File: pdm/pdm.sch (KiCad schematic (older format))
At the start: 30 parts, among them J1 Conn_01x04_Male, J2 Conn_01x12_Male, J3 Conn_01x04_Female, J4 Conn_01x06_Female, M1 Fan, M2 Fan, Q11 Q_PMOS_DSG, SW1 SW_Push, U2 SN65HVD233, U3 STM32F042G6Ux

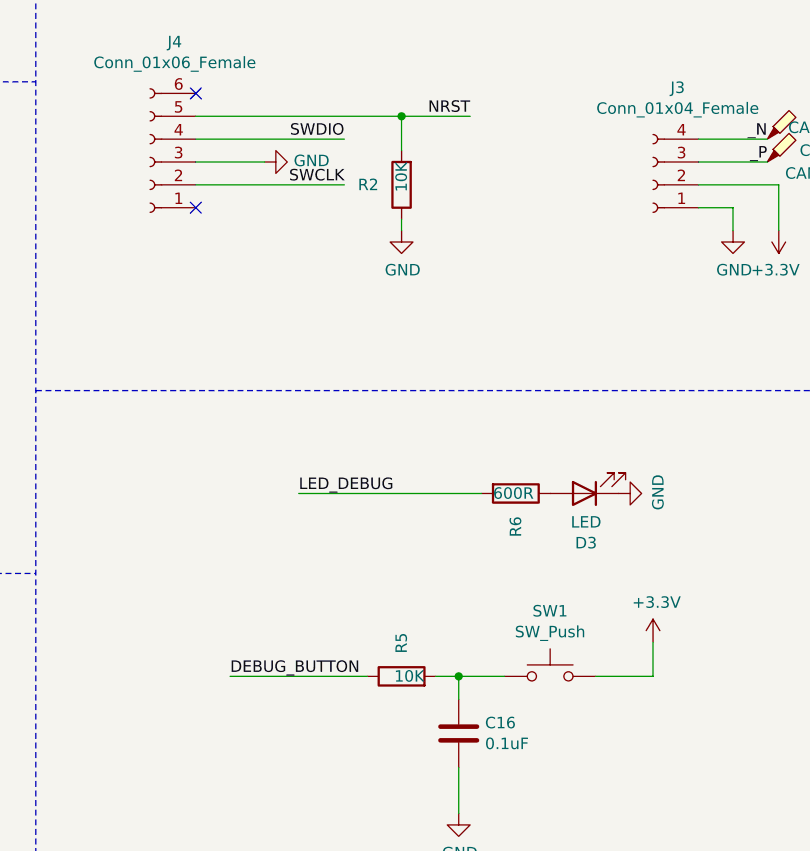
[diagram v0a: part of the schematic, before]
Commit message: added digikey BoM
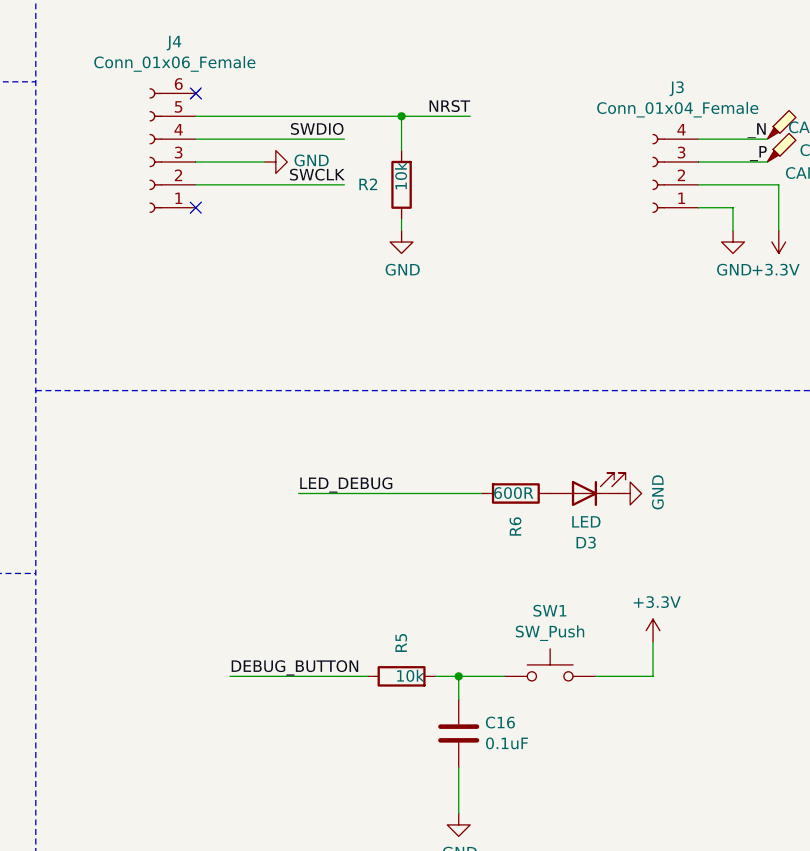
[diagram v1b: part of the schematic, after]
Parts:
- C10: Digi-Key_PN (none) -> 1276-1244-1-ND
- D3: Digi-Key_PN (none) -> 516-1431-1-ND
- J1: Digi-Key_PN (none) -> 1734-1024-ND
- J2: Digi-Key_PN (none) -> 1734-1635-ND
- J3: Digi-Key_PN (none) -> S5596-ND
- J4: Digi-Key_PN (none) -> S5598-ND
- M1, M2: Digi-Key_PN (none) -> 455-1657-ND
- Q11: Digi-Key_PN (none) -> SUD50P04-08-GE3CT-ND
- R2, R5: value 10K -> 10k; Digi-Key_PN (none) -> RNCP0805FTD10K0CT-ND
- R4: Digi-Key_PN (none) -> A129738CT-ND
- R6: Digi-Key_PN (none) -> A126352CT-ND
- SW1: Digi-Key_PN (none) -> 450-1650-ND
- U2: Digi-Key_PN (none) -> 296-35967-1-ND
- U3: Digi-Key_PN (none) -> 497-17345-ND
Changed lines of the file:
@@
 F 2 "Capacitor_SMD:C_0805_2012Metric_Pad1.18x1.45mm_HandSolder" H 3338 5500 50  0001 C CNN
 F 3 "~" H 3300 5650 50  0001 C CNN
+F 4 "1276-1244-1-ND" H 3300 5650 50  0001 C CNN "Digi-Key_PN"
 	1    3300 5650
 	1    0    0    -1
@@
 F 2 "Package_SO:SOIC-8_3.9x4.9mm_P1.27mm" H 2450 2200 50  0001 C CNN
 F 3 "http://www.ti.com/lit/ds/symlink/sn65hvd234.pdf" H 2350 3100 50  0001 C CNN
+F 4 "296-35967-1-ND" H 2450 2700 50  0001 C CNN "Digi-Key_PN"
 	1    2450 2700
 	1    0    0    -1
@@
 F 2 "Package_DFN_QFN:QFN-28_4x4mm_P0.5mm" H 5150 5700 50  0001 R CNN
 F 3 "http://www.st.com/st-web-ui/static/active/en/resource/technical/document/datasheet/DM00105814.pdf" H 5750 6400 50  0001 C CNN
+F 4 "497-17345-ND" H 5750 6400 50  0001 C CNN "Digi-Key_PN"
 	1    5750 6400
 	1    0    0    -1
@@
 F 2 "LED_SMD:LED_0805_2012Metric_Pad1.15x1.40mm_HandSolder" H 9600 4500 50  0001 C CNN
 F 3 "~" H 9600 4500 50  0001 C CNN
+F 4 "516-1431-1-ND" H 9600 4500 50  0001 C CNN "Digi-Key_PN"
 	1    9600 4500
 	-1   0    0    1
@@
 F 2 "Resistor_SMD:R_0805_2012Metric_Pad1.20x1.40mm_HandSolder" V 9230 4500 50  0001 C CNN
 F 3 "~" H 9300 4500 50  0001 C CNN
+F 4 "A126352CT-ND" H 9300 4500 50  0001 C CNN "Digi-Key_PN"
 	1    9300 4500
 	0    1    1    0
@@
 F 2 "Button_Switch_THT:SW_PUSH_6mm" H 9450 5500 50  0001 C CNN
 F 3 "~" H 9450 5500 50  0001 C CNN
+F 4 "450-1650-ND" H 9450 5300 50  0001 C CNN "Digi-Key_PN"
 	1    9450 5300
 	1    0    0    -1
@@
 P 8800 5300
 F 0 "R5" H 8900 5300 50  0000 L CNN
-F 1 "10K" V 8800 5200 50  0000 L CNN
+F 1 "10k" V 8800 5200 50  0000 L CNN
 F 2 "Resistor_SMD:R_0805_2012Metric_Pad1.20x1.40mm_HandSolder" V 8730 5300 50  0001 C CNN
 F 3 "~" H 8800 5300 50  0001 C CNN
+F 4 "RNCP0805FTD10K0CT-ND" H 8800 5300 50  0001 C CNN "Digi-Key_PN"
 	1    8800 5300
 	0    -1   -1   0
@@
 F 2 "DT13-12PB-B016:TE_DT13-12PB-B016" H 10550 1050 50  0001 C CNN
 F 3 "~" H 10550 1050 50  0001 C CNN
+F 4 "1734-1635-ND" H 10550 1050 50  0001 C CNN "Digi-Key_PN"
 	1    10550 1050
 	0    1    1    0
@@
 P 8800 3150
 F 0 "R2" H 8900 3150 50  0000 L CNN
-F 1 "10K" V 8800 3050 50  0000 L CNN
+F 1 "10k" V 8800 3050 50  0000 L CNN
 F 2 "Resistor_SMD:R_0805_2012Metric_Pad1.20x1.40mm_HandSolder" V 8730 3150 50  0001 C CNN
 F 3 "~" H 8800 3150 50  0001 C CNN
+F 4 "RNCP0805FTD10K0CT-ND" H 8800 3150 50  0001 C CNN "Digi-Key_PN"
 	1    8800 3150
 	-1   0    0    1
@@
 F 2 "DT13-4P:TE_DT13-4P" H 7600 1100 50  0001 C CNN
 F 3 "~" H 7600 1100 50  0001 C CNN
+F 4 "1734-1024-ND" H 7600 1100 50  0001 C CNN "Digi-Key_PN"
 	1    7600 1100
 	1    0    0    -1
@@
 F 2 "Capacitor_SMD:C_0805_2012Metric_Pad1.18x1.45mm_HandSolder" V 2980 2750 50  0001 C CNN
 F 3 "~" H 3050 2750 50  0001 C CNN
+F 4 "A129738CT-ND" H 3050 2750 50  0001 C CNN "Digi-Key_PN"
 	1    3050 2750
 	1    0    0    -1
@@
 F 2 "Connector_PinSocket_2.54mm:PinSocket_1x06_P2.54mm_Vertical_SMD_Pin1Left" H 7700 3050 50  0001 C CNN
 F 3 "~" H 7700 3050 50  0001 C CNN
+F 4 "S5598-ND" H 7700 3050 50  0001 C CNN "Digi-Key_PN"
 	1    7700 3050
 	-1   0    0    1
@@
 F 2 "Connector_PinSocket_2.54mm:PinSocket_1x04_P2.54mm_Vertical_SMD_Pin1Left" H 9900 3150 50  0001 C CNN
 F 3 "~" H 9900 3150 50  0001 C CNN
+F 4 "S5596-ND" H 9900 3150 50  0001 C CNN "Digi-Key_PN"
 	1    9900 3150
 	-1   0    0    1
@@
 F 2 "Package_TO_SOT_SMD:TO-252-2" H 8900 1500 50  0001 C CNN
 F 3 "https://www.vishay.com/docs/65594/sud50p04-08.pdf" H 8700 1400 50  0001 C CNN
+F 4 "SUD50P04-08-GE3CT-ND" H 8700 1400 50  0001 C CNN "Digi-Key_PN"
 	1    8700 1400
 	0    -1   -1   0
@@
 F 2 "Connector_JST:JST_EH_B2B-EH-A_1x02_P2.50mm_Vertical" H 5100 3810 50  0001 C CNN
 F 3 "~" H 5100 3810 50  0001 C CNN
+F 4 "455-1657-ND" H 5100 3800 50  0001 C CNN "Digi-Key_PN"
 	1    5100 3800
 	1    0    0    -1
@@
 F 2 "Connector_JST:JST_EH_B2B-EH-A_1x02_P2.50mm_Vertical" H 6200 3810 50  0001 C CNN
 F 3 "~" H 6200 3810 50  0001 C CNN
+F 4 "455-1657-ND" H 6200 3800 50  0001 C CNN "Digi-Key_PN"
 	1    6200 3800
 	1    0    0    -1

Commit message: added fixes for issue #11 #12 & #13
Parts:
- removed Q11: Q_PMOS_DSG, Package_TO_SOT_SMD:TO-252-2, symbol Device:Q_PMOS_GDS
- added D9: D, digikey-footprints:DO-214AB, symbol Device:D
- C16, C2, C7, C9: Digi-Key_PN CL21B104KBCNNNC -> 1276-1003-1-ND
- C4, C5: Digi-Key_PN 08051A200JAT2A -> 478-3735-1-ND
- C8: Digi-Key_PN T494A106M020AT -> 1276-6471-1-ND
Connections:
- wire segments 126 -> 127
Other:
- note added: "add est / suppression diode in paralell with vin"
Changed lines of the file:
@@
 F 2 "Capacitor_SMD:C_0805_2012Metric_Pad1.18x1.45mm_HandSolder" H 1238 3700 50  0001 C CNN
 F 3 "~" H 1200 3850 50  0001 C CNN
-F 4 "08051A200JAT2A" H 1200 3850 50  0001 C CNN "Digi-Key_PN"
+F 4 "478-3735-1-ND" H 1200 3850 50  0001 C CNN "Digi-Key_PN"
 	1    1200 3850
 	0    -1   -1   0
@@
 F 2 "Capacitor_SMD:C_0805_2012Metric_Pad1.18x1.45mm_HandSolder" H 1238 4400 50  0001 C CNN
 F 3 "~" H 1200 4550 50  0001 C CNN
-F 4 "08051A200JAT2A" H 1200 4550 50  0001 C CNN "Digi-Key_PN"
+F 4 "478-3735-1-ND" H 1200 4550 50  0001 C CNN "Digi-Key_PN"
 	1    1200 4550
 	0    -1   -1   0
@@
 F 2 "Capacitor_SMD:C_0805_2012Metric_Pad1.18x1.45mm_HandSolder" H 2038 5500 50  0001 C CNN
 F 3 "~" H 2000 5650 50  0001 C CNN
-F 4 "T494A106M020AT" H 2000 5650 50  0001 C CNN "Digi-Key_PN"
+F 4 "1276-6471-1-ND" H 2000 5650 50  0001 C CNN "Digi-Key_PN"
 	1    2000 5650
 	1    0    0    -1
@@
 F 2 "Capacitor_SMD:C_0805_2012Metric_Pad1.18x1.45mm_HandSolder" H 1138 2550 50  0001 C CNN
 F 3 "~" H 1100 2700 50  0001 C CNN
-F 4 "CL21B104KBCNNNC" H 1100 2700 50  0001 C CNN "Digi-Key_PN"
+F 4 "1276-1003-1-ND" H 1100 2700 50  0001 C CNN "Digi-Key_PN"
 	1    1100 2700
 	1    0    0    -1
@@
 F 2 "Capacitor_SMD:C_0805_2012Metric_Pad1.18x1.45mm_HandSolder" H 1538 5500 50  0001 C CNN
 F 3 "~" H 1500 5650 50  0001 C CNN
-F 4 "CL21B104KBCNNNC" H 1500 5650 50  0001 C CNN "Digi-Key_PN"
+F 4 "1276-1003-1-ND" H 1500 5650 50  0001 C CNN "Digi-Key_PN"
 	1    1500 5650
 	1    0    0    -1
@@
 F 2 "Capacitor_SMD:C_0805_2012Metric_Pad1.18x1.45mm_HandSolder" H 2638 5500 50  0001 C CNN
 F 3 "~" H 2600 5650 50  0001 C CNN
-F 4 "CL21B104KBCNNNC" H 2600 5650 50  0001 C CNN "Digi-Key_PN"
+F 4 "1276-1003-1-ND" H 2600 5650 50  0001 C CNN "Digi-Key_PN"
 	1    2600 5650
 	1    0    0    -1
@@
 $EndComp
 Wire Wire Line
-	7800 1000 8350 1000
+	7800 1000 9450 1000
 $Comp
 L power:GND #PWR0109
 U 1 1 6002F9F5
-P 8350 1000
-F 0 "#PWR0109" H 8350 750 50  0001 C CNN
-F 1 "GND" V 8355 872 50  0000 R CNN
-F 2 "" H 8350 1000 50  0001 C CNN
-F 3 "" H 8350 1000 50  0001 C CNN
-	1    8350 1000
+P 9450 1000
+F 0 "#PWR0109" H 9450 750 50  0001 C CNN
+F 1 "GND" V 9455 872 50  0000 R CNN
+F 2 "" H 9450 1000 50  0001 C CNN
+F 3 "" H 9450 1000 50  0001 C CNN
+	1    9450 1000
 	0    -1   -1   0
 $EndComp
@@
 F 2 "Capacitor_SMD:C_0805_2012Metric_Pad1.18x1.45mm_HandSolder" H 9088 5400 50  0001 C CNN
 F 3 "~" H 9050 5550 50  0001 C CNN
-F 4 "CL21B104KBCNNNC" H 9050 5550 50  0001 C CNN "Digi-Key_PN"
+F 4 "1276-1003-1-ND" H 9050 5550 50  0001 C CNN "Digi-Key_PN"
 	1    9050 5550
 	1    0    0    -1
@@
 Text Label 4450 6900 0    50   ~ 0
 fuse5
-$Comp
-L pdm-rescue:GND-power #PWR0108
-U 1 1 60324A05
-P 8700 1800
-F 0 "#PWR0108" H 8700 1550 50  0001 C CNN
-F 1 "GND" H 8705 1627 50  0000 C CNN
-F 2 "" H 8700 1800 50  0001 C CNN
-F 3 "" H 8700 1800 50  0001 C CNN
-	1    8700 1800
-	1    0    0    -1
-$EndComp
-Wire Wire Line
-	8700 1800 8700 1600
-Wire Wire Line
-	8500 1300 7850 1300
 Wire Wire Line
 	7800 1100 7850 1100
@@
 Wire Wire Line
 	7850 1200 7850 1300
-Wire Wire Line
-	9450 1300 8900 1300
-$Comp
-L Device:Q_PMOS_GDS Q11
-U 1 1 60318C08
-P 8700 1400
-F 0 "Q11" V 9042 1400 50  0000 C CNN
-F 1 "Q_PMOS_DSG" V 8951 1400 50  0000 C CNN
-F 2 "Package_TO_SOT_SMD:TO-252-2" H 8900 1500 50  0001 C CNN
-F 3 "https://www.vishay.com/docs/65594/sud50p04-08.pdf" H 8700 1400 50  0001 C CNN
-F 4 "SUD50P04-08-GE3CT-ND" H 8700 1400 50  0001 C CNN "Digi-Key_PN"
-	1    8700 1400
-	0    -1   -1   0
-$EndComp
 Text Label 8100 1300 0    50   ~ 0
 vin
@@
 NoConn ~ 7900 2750
 NoConn ~ 7900 3250
+Text Notes 8050 650  0    50   ~ 0
+add est / suppression diode in paralell with vin
+Wire Wire Line
+	7850 1300 8650 1300
+$Comp
+L power:GND #PWR0108
+U 1 1 601AB2EC
+P 8650 1900
+F 0 "#PWR0108" H 8650 1650 50  0001 C CNN
+F 1 "GND" V 8655 1772 50  0000 R CNN
+F 2 "" H 8650 1900 50  0001 C CNN
+F 3 "" H 8650 1900 50  0001 C CNN
+	1    8650 1900
+	1    0    0    -1
+$EndComp
+Wire Wire Line
+	8650 1300 8650 1450
+Wire Wire Line
+	8650 1750 8650 1900
+Connection ~ 8650 1300
+Wire Wire Line
+	8650 1300 9450 1300
+$Comp
+L Device:D D9
+U 1 1 601BD890
+P 8650 1600
+F 0 "D9" V 8604 1680 50  0000 L CNN
+F 1 "D" V 8695 1680 50  0000 L CNN
+F 2 "digikey-footprints:DO-214AB" H 8650 1600 50  0001 C CNN
+F 3 "https://www.littelfuse.com/~/media/electronics/datasheets/tvs_diodes/littelfuse_tvs_diode_5_0smdj_datasheet.pdf.pdf" H 8650 1600 50  0001 C CNN
+F 4 "5.0SMDJ28ACT-ND" H 8650 1600 50  0001 C CNN "Digi-Key_PN"
+	1    8650 1600
+	0    1    1    0
+$EndComp
 $EndSCHEMATC

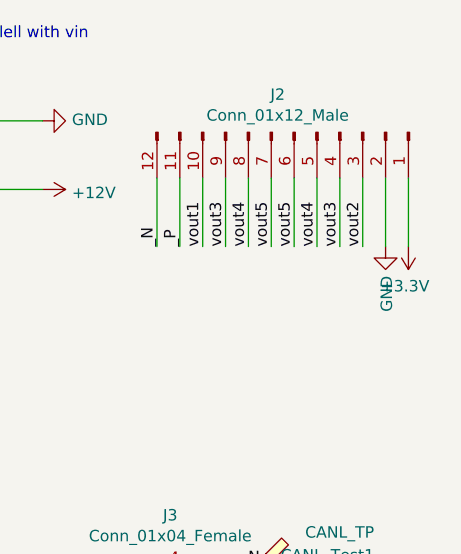
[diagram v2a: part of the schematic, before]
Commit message: removed 3v3 w/ gnd on out
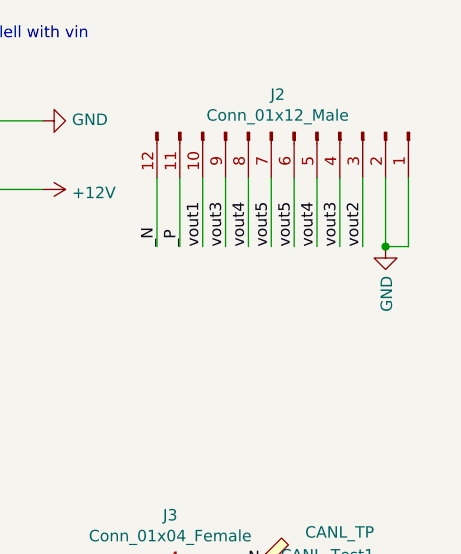
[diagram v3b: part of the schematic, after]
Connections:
- wire segments 127 -> 128
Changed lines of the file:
@@
 Wire Wire Line
 	11050 1250 11050 1550
-$Comp
-L pdm-rescue:+3.3V-power #PWR0117
-U 1 1 60219DD9
-P 11050 1550
-F 0 "#PWR0117" H 11050 1400 50  0001 C CNN
-F 1 "+3.3V" H 11065 1723 50  0000 C CNN
-F 2 "" H 11050 1550 50  0001 C CNN
-F 3 "" H 11050 1550 50  0001 C CNN
-	1    11050 1550
-	-1   0    0    1
-$EndComp
 Wire Wire Line
 	10950 1250 10950 1550
@@
 	0    1    1    0
 $EndComp
+Wire Wire Line
+	10950 1550 11050 1550
+Connection ~ 10950 1550
 $EndSCHEMATC

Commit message: Fixed LED Work
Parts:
- C10: Mouser PN (none) -> 603-CC0805KFX5R8BB47
- C16, C2, C7, C9: Mouser PN (none) -> 603-CC0805MRX77BB104
- C4, C5: Mouser PN (none) -> 603-CC805JRNPO9BN160
- C8: Mouser PN (none) -> 603-CC0805MKX58BB105
- D3: Mouser PN (none) -> 630-HSMA-C170-T0000
- D9: Mouser PN (none) -> 576-5.0SMDJ28A
- J1: Mouser PN (none) -> 571-DT13-4P
- J2: Mouser PN (none) -> 571-DT13-12PB-B016
- R2, R5: Mouser PN (none) -> 603-AC0805FR-0710K5L
- R4: Mouser PN (none) -> 279-CPF-A-0805B120RE
- R6: value 600R -> 120R; Mouser PN (none) -> 603-RC0805JR-07120RL
- U2: Mouser PN (none) -> 595-SN65HVD233QDRQ1
- U3: Mouser PN (none) -> 511-STM32F042G6U6
- XTAL1: Mouser PN (none) -> 344-NX3225GD8MCRA3
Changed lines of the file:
@@
 F 3 "~" H 1200 3850 50  0001 C CNN
 F 4 "478-3735-1-ND" H 1200 3850 50  0001 C CNN "Digi-Key_PN"
+F 5 "603-CC805JRNPO9BN160" H 1200 3850 50  0001 C CNN "Mouser PN"
 	1    1200 3850
 	0    -1   -1   0
@@
 F 3 "~" H 1200 4550 50  0001 C CNN
 F 4 "478-3735-1-ND" H 1200 4550 50  0001 C CNN "Digi-Key_PN"
+F 5 "603-CC805JRNPO9BN160" H 1200 4550 50  0001 C CNN "Mouser PN"
 	1    1200 4550
 	0    -1   -1   0
@@
 F 3 "~" H 3300 5650 50  0001 C CNN
 F 4 "1276-1244-1-ND" H 3300 5650 50  0001 C CNN "Digi-Key_PN"
+F 5 "603-CC0805KFX5R8BB47" H 3300 5650 50  0001 C CNN "Mouser PN"
 	1    3300 5650
 	1    0    0    -1
@@
 F 3 "~" H 2000 5650 50  0001 C CNN
 F 4 "1276-6471-1-ND" H 2000 5650 50  0001 C CNN "Digi-Key_PN"
+F 5 "603-CC0805MKX58BB105" H 2000 5650 50  0001 C CNN "Mouser PN"
 	1    2000 5650
 	1    0    0    -1
@@
 F 3 "~" H 1100 2700 50  0001 C CNN
 F 4 "1276-1003-1-ND" H 1100 2700 50  0001 C CNN "Digi-Key_PN"
+F 5 "603-CC0805MRX77BB104" H 1100 2700 50  0001 C CNN "Mouser PN"
 	1    1100 2700
 	1    0    0    -1
@@
 F 3 "http://www.ti.com/lit/ds/symlink/sn65hvd234.pdf" H 2350 3100 50  0001 C CNN
 F 4 "296-35967-1-ND" H 2450 2700 50  0001 C CNN "Digi-Key_PN"
+F 5 "595-SN65HVD233QDRQ1" H 2450 2700 50  0001 C CNN "Mouser PN"
 	1    2450 2700
 	1    0    0    -1
@@
 F 3 "~" H 1500 5650 50  0001 C CNN
 F 4 "1276-1003-1-ND" H 1500 5650 50  0001 C CNN "Digi-Key_PN"
+F 5 "603-CC0805MRX77BB104" H 1500 5650 50  0001 C CNN "Mouser PN"
 	1    1500 5650
 	1    0    0    -1
@@
 F 3 "~" H 2600 5650 50  0001 C CNN
 F 4 "1276-1003-1-ND" H 2600 5650 50  0001 C CNN "Digi-Key_PN"
+F 5 "603-CC0805MRX77BB104" H 2600 5650 50  0001 C CNN "Mouser PN"
 	1    2600 5650
 	1    0    0    -1
@@
 F 3 "http://www.st.com/st-web-ui/static/active/en/resource/technical/document/datasheet/DM00105814.pdf" H 5750 6400 50  0001 C CNN
 F 4 "497-17345-ND" H 5750 6400 50  0001 C CNN "Digi-Key_PN"
+F 5 "511-STM32F042G6U6" H 5750 6400 50  0001 C CNN "Mouser PN"
 	1    5750 6400
 	1    0    0    -1
@@
 F 3 "~" H 9600 4500 50  0001 C CNN
 F 4 "516-1431-1-ND" H 9600 4500 50  0001 C CNN "Digi-Key_PN"
+F 5 "630-HSMA-C170-T0000" H 9600 4500 50  0001 C CNN "Mouser PN"
 	1    9600 4500
 	-1   0    0    1
@@
 P 9300 4500
 F 0 "R6" H 9400 4500 50  0000 L CNN
-F 1 "600R" V 9300 4400 50  0000 L CNN
+F 1 "120R" V 9300 4400 50  0000 L CNN
 F 2 "Resistor_SMD:R_0805_2012Metric_Pad1.20x1.40mm_HandSolder" V 9230 4500 50  0001 C CNN
 F 3 "~" H 9300 4500 50  0001 C CNN
 F 4 "A126352CT-ND" H 9300 4500 50  0001 C CNN "Digi-Key_PN"
+F 5 "603-RC0805JR-07120RL" H 9300 4500 50  0001 C CNN "Mouser PN"
 	1    9300 4500
 	0    1    1    0
@@
 F 3 "~" H 8800 5300 50  0001 C CNN
 F 4 "RNCP0805FTD10K0CT-ND" H 8800 5300 50  0001 C CNN "Digi-Key_PN"
+F 5 "603-AC0805FR-0710K5L" H 8800 5300 50  0001 C CNN "Mouser PN"
 	1    8800 5300
 	0    -1   -1   0
@@
 F 3 "~" H 10550 1050 50  0001 C CNN
 F 4 "1734-1635-ND" H 10550 1050 50  0001 C CNN "Digi-Key_PN"
+F 5 "571-DT13-12PB-B016" H 10550 1050 50  0001 C CNN "Mouser PN"
 	1    10550 1050
 	0    1    1    0
@@
 F 3 "~" H 8800 3150 50  0001 C CNN
 F 4 "RNCP0805FTD10K0CT-ND" H 8800 3150 50  0001 C CNN "Digi-Key_PN"
+F 5 "603-AC0805FR-0710K5L" H 8800 3150 50  0001 C CNN "Mouser PN"
 	1    8800 3150
 	-1   0    0    1
@@
 F 3 "~" H 7600 1100 50  0001 C CNN
 F 4 "1734-1024-ND" H 7600 1100 50  0001 C CNN "Digi-Key_PN"
+F 5 "571-DT13-4P" H 7600 1100 50  0001 C CNN "Mouser PN"
 	1    7600 1100
 	1    0    0    -1
@@
 F 3 "~" H 9050 5550 50  0001 C CNN
 F 4 "1276-1003-1-ND" H 9050 5550 50  0001 C CNN "Digi-Key_PN"
+F 5 "603-CC0805MRX77BB104" H 9050 5550 50  0001 C CNN "Mouser PN"
 	1    9050 5550
 	1    0    0    -1
@@
 F 3 "~" H 3050 2750 50  0001 C CNN
 F 4 "A129738CT-ND" H 3050 2750 50  0001 C CNN "Digi-Key_PN"
+F 5 "279-CPF-A-0805B120RE" H 3050 2750 50  0001 C CNN "Mouser PN"
 	1    3050 2750
 	1    0    0    -1
@@
 F 11 "NDK America, Inc." H 1650 5300 60  0001 L CNN "Manufacturer"
 F 12 "Active" H 1650 5400 60  0001 L CNN "Status"
+F 13 "344-NX3225GD8MCRA3" H 1450 4200 50  0001 C CNN "Mouser PN"
 	1    1450 4200
 	0    1    1    0
@@
 F 3 "https://www.littelfuse.com/~/media/electronics/datasheets/tvs_diodes/littelfuse_tvs_diode_5_0smdj_datasheet.pdf.pdf" H 8650 1600 50  0001 C CNN
 F 4 "5.0SMDJ28ACT-ND" H 8650 1600 50  0001 C CNN "Digi-Key_PN"
+F 5 "576-5.0SMDJ28A" H 8650 1600 50  0001 C CNN "Mouser PN"
 	1    8650 1600
 	0    1    1    0

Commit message: changed oscilltor and exposed themral pads
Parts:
- removed XTAL1: NX3225GD-8MHZ-STD-CRA-3, digikey-footprints:SMD-2_3.2x2.5mm, symbol dk_Crystals:NX3225GD-8MHZ-STD-CRA-3
- added RarePepe1: RarePepe, pdm_v2:rarepepe, symbol Mechanical:MountingHole
- added Y1: Crystal_GND24, Crystal:Crystal_SMD_3225-4Pin_3.2x2.5mm_HandSoldering, symbol Device:Crystal_GND24
- renumbered C2 to C1, C4 to C2, C5 to C3, C7 to C4, C8 to C5, C9 to C6, C10 to C7, C16 to C8, D9 to D1, D3 to D2, J4 to J2, J2 to J4, R4 to R1, R5 to R3, R6 to R4, U2 to U1, U3 to U2
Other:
- moved on the sheet: C2, C3
